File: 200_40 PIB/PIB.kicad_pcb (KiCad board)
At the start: 4 copper layers, 80 x 49 mm, 234 parts, among them J1 M80-5100442, J10 53398-0671, J11 53398-0271, J12 M80-5100842, J13 53398-0271, J15 53398-0571, J2 53398-0471, J3 G125-MS12605M2P, J4 53398-0671, J5 53398-1371, J6 MMCX, J7 MMCX, J8 SWD/DEBUG, J9 53398-0671, Q1 Si7489DP, Q10 IRF7832, Q11 IRF7832, Q2 Si7489DP, Q9 IRF7832, SW1 B3F-1000, U1 LT3065EDDPBF, U10 LT8580EDD, U11 OP37, U12 MAX823TEUK_T, U13 74LVC1G18DBV, U14 74HC08PW, U15 74HC08PW, U16 74LVC2G157DCU, U17 74LVC1G18DBV, U2 MIC4424YM, U3 MIC4424YM, U4 STM32G431RBTx, U5 ADM1270ACPZ, U6 LM1117MP-3.3, U7 ADM1270ACPZ, U8 74LVC1GU04DRL, U9 74LVC2G126DCU, Y1 ABM3B-8.000MHZ-10-D1G-T

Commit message: LADS WE ARE FUCKED
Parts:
- removed R10, R11, R12, R43, R5, R60: 1K, Resistor_SMD:R_0402_1005Metric
- removed R44: 100K, Resistor_SMD:R_0402_1005Metric
- removed R59: 33K, Resistor_SMD:R_0402_1005Metric
- removed R61: 2K, Resistor_SMD:R_0402_1005Metric
- added C69: 4.7uF, Capacitor_SMD:C_0603_1608Metric, F.Cu at (204.8, 47.1)
- added C70: 1uF, Capacitor_SMD:C_0603_1608Metric, F.Cu at (204.8, 49.6)
- added C71: 470pF, Capacitor_SMD:C_0402_1005Metric, F.Cu at (208.2, 46.9)
- added C72: 470pF, Capacitor_SMD:C_0402_1005Metric, F.Cu at (208.2, 48.8)
- added C73: 1uF, Capacitor_SMD:C_0402_1005Metric, F.Cu at (223.3, 64.9)
- added C74: 1uF, Capacitor_SMD:C_0402_1005Metric, F.Cu at (223.3, 66.8)
- added C75: 100nF, Capacitor_SMD:C_0402_1005Metric, F.Cu at (223.3, 68.8)
- added C76: 100nF, Capacitor_SMD:C_0402_1005Metric, F.Cu at (207.7, 64.9)
- added C77: 100nF, Capacitor_SMD:C_0402_1005Metric, F.Cu at (207.7, 66.8)
- added C78: 1uF, Capacitor_SMD:C_0603_1608Metric, F.Cu at (204.3, 65.1)
- added C79: 1uF, Capacitor_SMD:C_0603_1608Metric, F.Cu at (204.3, 67.6)
- added C80: 100nF, Capacitor_SMD:C_0402_1005Metric, F.Cu at (207.7, 68.8)
- added C81: 22nF, Capacitor_SMD:C_0402_1005Metric, F.Cu at (207.7, 70.8)
- added C82: 1uF, Capacitor_SMD:C_0603_1608Metric, F.Cu at (204.3, 70.2)
- added D11: NSVR1020MW2T1G, Diode_SMD:D_SOD-323, F.Cu at (214.8, 65.3)
- added D36: NSVR1020MW2T1G, Diode_SMD:D_SOD-323, F.Cu at (214.8, 68.3)
- added D37: NSVR1020MW2T1G, Diode_SMD:D_SOD-323, F.Cu at (214.8, 71.2)
- added D38: SD12C-01F, Diode_SMD:D_SOD-323, F.Cu at (195.7, 47.3)
- added D39: BAT54J, Diode_SMD:D_SOD-323F, F.Cu at (195.7, 50.3)
- added D40: BAT54J, Diode_SMD:D_SOD-323F, F.Cu at (195.7, 53.2)
- added D41: BAT54J, Diode_SMD:D_SOD-323F, F.Cu at (214.8, 74.2)
- added D42: BAT54J, Diode_SMD:D_SOD-323F, F.Cu at (214.8, 77.2)
- added D43: BAT54J, Diode_SMD:D_SOD-323F, F.Cu at (195.7, 56.2)
- added D44: BAT54J, Diode_SMD:D_SOD-323F, F.Cu at (195.7, 59.1)
- added D45: PESD3V3U1UL, Diode_SMD:D_SOD-882, F.Cu at (203.7, 75.1)
- added D46: PESD3V3U1UL, Diode_SMD:D_SOD-882, F.Cu at (203.7, 77.4)
- added D47: BAT54C, Package_TO_SOT_SMD:SOT-23, F.Cu at (219.4, 66.1)
- added D48: BAT54C, Package_TO_SOT_SMD:SOT-23, F.Cu at (219.4, 70.5)
- added D49: PESD3V3U1UL, Diode_SMD:D_SOD-882, F.Cu at (203.7, 79.8)
- added D50: BAT54C, Package_TO_SOT_SMD:SOT-23, F.Cu at (219.4, 75.0)
- added JP1: WD_ENABLE, Jumper:SolderJumper-2_P1.3mm_Open_Pad1.0x1.5mm, F.Cu at (207.2, 81.0)
- added Q3: BSS138, Package_TO_SOT_SMD:SOT-23, F.Cu at (200.3, 48.1)
- added Q4: BSS138, Package_TO_SOT_SMD:SOT-23, F.Cu at (200.3, 52.5)
- added Q5: BSS138, Package_TO_SOT_SMD:SOT-23, F.Cu at (200.3, 57.0)
- added Q6: Si7489DP, Package_SO:PowerPAK_SO-8_Single, F.Cu at (198.0, 79.1)
- added R100: 100R, Resistor_SMD:R_0402_1005Metric, F.Cu at (207.1, 56.9)
- added R101: 10K, Resistor_SMD:R_0402_1005Metric, F.Cu at (207.1, 58.9)
- added R102: 100R, Resistor_SMD:R_0402_1005Metric, F.Cu at (207.1, 60.9)
- added R103: 1K, Resistor_SMD:R_0402_1005Metric, F.Cu at (195.0, 66.9)
- added R104: 1K, Resistor_SMD:R_0402_1005Metric, F.Cu at (210.0, 56.9)
- added R105: 1K, Resistor_SMD:R_0402_1005Metric, F.Cu at (210.0, 58.9)
- added R106: 100R, Resistor_SMD:R_0402_1005Metric, F.Cu at (210.0, 60.9)
- added R107: 100K, Resistor_SMD:R_0402_1005Metric, F.Cu at (223.3, 75.4)
- added R108: 1K, Resistor_SMD:R_0402_1005Metric, F.Cu at (195.0, 68.8)
- added R109: 10K, Resistor_SMD:R_0402_1005Metric, F.Cu at (195.0, 70.8)
- added R110: 100R, Resistor_SMD:R_0402_1005Metric, F.Cu at (223.3, 77.4)
- added R111: 33K, Resistor_SMD:R_0402_1005Metric, F.Cu at (195.0, 72.8)
- added R112: 1K, Resistor_SMD:R_0402_1005Metric, F.Cu at (195.0, 74.8)
- added R113: 2K, Resistor_SMD:R_0402_1005Metric, F.Cu at (197.9, 64.9)
- added R114: 10K, Resistor_SMD:R_0402_1005Metric, F.Cu at (197.9, 66.9)
- added R115: 100K, Resistor_SMD:R_0402_1005Metric, F.Cu at (197.9, 68.8)
- added R116: 0R, Resistor_SMD:R_0402_1005Metric, F.Cu at (197.9, 70.8)
- added R117: 100K, Resistor_SMD:R_0402_1005Metric, F.Cu at (197.9, 72.8)
- added R118: 10K, Resistor_SMD:R_0402_1005Metric, F.Cu at (197.9, 74.8)
- added R119: 10K, Resistor_SMD:R_0402_1005Metric, F.Cu at (200.8, 64.9)
- added R120: 1K, Resistor_SMD:R_0402_1005Metric, F.Cu at (200.8, 66.9)
- added R121: 10K, Resistor_SMD:R_0402_1005Metric, F.Cu at (200.8, 68.8)
- added R122: 59K, Resistor_SMD:R_0402_1005Metric, F.Cu at (214.9, 54.8)
- added R123: 107K, Resistor_SMD:R_0402_1005Metric, F.Cu at (214.9, 56.8)
- added R124: 100K, Resistor_SMD:R_0402_1005Metric, F.Cu at (200.8, 70.8)
- added R125: 150K, Resistor_SMD:R_0402_1005Metric, F.Cu at (200.8, 72.8)
- added R126: 158K, Resistor_SMD:R_0402_1005Metric, F.Cu at (214.9, 46.9)
- added R127: 3.92K, Resistor_SMD:R_0402_1005Metric, F.Cu at (214.9, 48.9)
- added R128: 9.53K, Resistor_SMD:R_0402_1005Metric, F.Cu at (214.9, 50.8)
- added R88: 10K, Resistor_SMD:R_0402_1005Metric, F.Cu at (195.0, 64.9)
- added R89: 10K, Resistor_SMD:R_0402_1005Metric, F.Cu at (219.8, 46.9)
- added R90: 10K, Resistor_SMD:R_0402_1005Metric, F.Cu at (219.8, 48.9)
- added R91: 10K, Resistor_SMD:R_0402_1005Metric, F.Cu at (219.8, 50.8)
- added R92: 10K, Resistor_SMD:R_0402_1005Metric, F.Cu at (219.8, 52.8)
- added R93: 10K, Resistor_SMD:R_0402_1005Metric, F.Cu at (219.8, 54.8)
- added R94: 10K, Resistor_SMD:R_0402_1005Metric, F.Cu at (219.8, 56.8)
- added R95: 100K, Resistor_SMD:R_0603_1608Metric, F.Cu at (204.8, 52.1)
- added R96: 10K, Resistor_SMD:R_0402_1005Metric, F.Cu at (204.2, 56.9)
- added R97: 10K, Resistor_SMD:R_0402_1005Metric, F.Cu at (204.2, 58.9)
- added R98: 1M, Resistor_SMD:R_0603_1608Metric, F.Cu at (204.8, 54.6)
- added R99: 10K, Resistor_SMD:R_0402_1005Metric, F.Cu at (204.2, 60.9)
- added TH1: 3435K 10K, Resistor_SMD:R_0603_1608Metric, F.Cu at (204.3, 72.7)
- added U18: 74LVC2G14, Package_TO_SOT_SMD:SOT-23-6, F.Cu at (224.4, 72.2)
- added U19: ADM1270ACPZ, Package_CSP:LFCSP-16-1EP_3x3mm_P0.5mm_EP1.5x1.5mm, F.Cu at (208.0, 76.6)
- C26, C27: value 27pF -> 12pF
- C29, C34: value 10nF -> 100nF
- C45: value TBD -> 10nF C0G
- D18: value PESD5V0S1UL -> LED; footprint Diode_SMD:D_SOD-882 -> LED_SMD:LED_0603_1608Metric
- R17: value 1.13K -> 1K
- R18: value 21.5K -> 20K
- R35: value 15m -> 10m
- R38: value 1K -> 10m; footprint Resistor_SMD:R_0402_1005Metric -> Resistor_SMD:R_0805_2012Metric
- R45: value 10K -> 100K; footprint Resistor_SMD:R_0603_1608Metric -> Resistor_SMD:R_0402_1005Metric
- R46: value 43K -> 1K; footprint Resistor_SMD:R_0603_1608Metric -> Resistor_SMD:R_0402_1005Metric
- R47: value 1K -> 100K
- R48: value 2K -> 9.53K
- R49: value 1K -> 3.92K
- R50: value 33K -> 158K
- R57: value 33K -> 100K
- R79: value TBD -> 2K
- SW1: value B3F-1000 -> SKRKAHE020; footprint Button_Switch_THT:SW_PUSH_6mm -> Button_Switch_SMD:SW_Push_SPST_NO_Alps_SKRK
- U11: value OP37 -> OP27
- U8: value 74LVC1GU04DRL -> 74AHC1G125; footprint Package_TO_SOT_SMD:SOT-553 -> Package_TO_SOT_SMD:SOT-23-5
- U9: value 74LVC2G126DCU -> 74LVC2G17; footprint Package_SO:VSSOP-8_2.3x2mm_P0.5mm -> Package_TO_SOT_SMD:SOT-23-6
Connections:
- net /IGNITER_RST renamed /~{PD_RST}
- C1 pad 1: BAT_HOT -> VBAT_PROT
- C21 pad 1: Net-(U5-ISET) -> Net-(U5-VCAP)
- C22 pad 1: +12V -> Net-(D11-A)
- C28 pad 1: BAT_HOT -> VBAT_PROT
- C33 pad 1: BAT_HOT -> VBAT_PROT
- C45 pad 2: /ADC_I_DCHG -> Net-(Q3-S)
- C6 pad 1: +12V -> Net-(D11-A)
- C62 pad 1: BAT_HOT -> VBAT_PROT
- D18 pad 1: /ADC_V_DCHG -> GND
- D18 pad 2: GND -> Net-(D18-A)
- D3 pad 1: BAT_HOT -> VBAT_HOT
- J2 pad 2: BAT_HOT -> VBAT_PROT
- J2 pad 3: BAT_HOT -> VBAT_PROT
- J3 pad 1: BAT_HOT -> VBAT_HOT
- J3 pad 2: BAT_HOT -> VBAT_HOT
- J3 pad 3: BAT_HOT -> VBAT_HOT
- J6 pad 1: /ADC_V_DCHG -> /Rogowski Integrator/V_DCHG_IN
- J7 pad 1: Net-(J7-In) -> Net-(D38-A2)
- J8 pad 5: /nRST -> Net-(J8-Pin_5)
- R1 pad 1: BAT_HOT -> +3.3V
- R1 pad 2: Net-(U1-PWRGD) -> /12V_PG
- R18 pad 1: +12V -> Net-(D11-A)
- R29 pad 1: /IGNITER_PULSE_GATED -> /IGNITER_EXT
- R35 pad 2: BAT_HOT -> VBAT_PROT
- R38 pad 1: /VALVE1_H_GATED -> Net-(U19-SENSE-)
- R38 pad 2: Net-(U2-INB) -> VBAT_HOT
- R39 pad 1: Net-(U2-INB) -> /VALVE1_H_GATED
- R40 pad 1: Net-(U2-INA) -> /VALVE1_L_GATED
- R45 pad 1: GND -> /Valve Driver/EGSE_OPEN_F
- R45 pad 2: Net-(R45-Pad2) -> GND
- R46 pad 1: Net-(R45-Pad2) -> /Valve Driver/EGSE_OPEN_F
- R46 pad 2: 12V_GSE -> /OPEN/~{CLOSE}
- R47 pad 1: /OPEN/~{CLOSE} -> Net-(D41-K)
- R47 pad 2: Net-(Q10-G) -> GND
- R50 pad 2: BAT_HOT -> VBAT_PROT
- R65 pad 2: BAT_HOT -> VBAT_PROT
- R79 pad 1: Net-(J7-In) -> Net-(C69-Pad2)
- R82 pad 1: /RCC_LSCO -> /DPT_MCLK
- R86 pad 1: /RCC_LSCO -> /DPT_MCLK
- SW1 pad 1: GND -> Net-(U12-~{MR})
- SW1 pad 2: Net-(U12-~{MR}) -> GND
- U1 pad 1: BAT_HOT -> VBAT_PROT
- U1 pad 10: +12V -> Net-(D11-A)
- U1 pad 2: BAT_HOT -> VBAT_PROT
- U1 pad 3: BAT_HOT -> VBAT_PROT
- U1 pad 4: Net-(U1-PWRGD) -> /12V_PG
- U1 pad 9: +12V -> Net-(D11-A)
- U11 pad 3: GND -> Net-(U11A-+)
- U11 pad 6: /ADC_I_DCHG -> Net-(Q3-S)
- U12 pad 4: /WDG_IN -> Net-(JP1-B)
- U2 pad 2: Net-(U2-INA) -> /VALVE1_L_GATED
- U2 pad 4: Net-(U2-INB) -> /VALVE1_H_GATED
- U4 pad 14: /RCC_LSCO -> /12V_PG
- U4 pad 39: unconnected-(U4-PC7-Pad39) -> /DPT_MCLK
- U4 pad 44: unconnected-(U4-PA10-Pad44) -> /BAT_EN
- U4 pad 45: unconnected-(U4-PA11-Pad45) -> /BAT_PGOOD
- U4 pad 55: unconnected-(U4-PD2-Pad55) -> /DEBUG_LED
- U5 pad 1: Net-(U5-ISET) -> Net-(U5-VCAP)
- U5 pad 15: BAT_HOT -> VBAT_PROT
- U7 pad 15: BAT_HOT -> VBAT_PROT
- U8 pad 1: unconnected-(U8-NC-Pad1) -> GND
- U8 pad 2: Net-(R43-Pad2) -> /IGNITER_PULSE_GATED
- U8 pad 4: Net-(U8-Pad4) -> /IGNITER_EXT
- U8 pad 5: 3.3V_EGSE -> +3.3V
- U9 pad 1: Net-(R45-Pad2) -> Net-(D42-K)
- U9 pad 2: Net-(R43-Pad2) -> GND
- U9 pad 3: Net-(U3-INA) -> Net-(D41-K)
- U9 pad 4: GND -> Net-(D47-Pad1)
- U9 pad 5: Net-(U8-Pad4) -> 3.3V_EGSE
- U9 pad 6: Net-(U3-INB) -> Net-(D48-Pad1)
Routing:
- net (no net): track 0.00 -> 63.3 mm, vias 0 -> 3
- net /RCC_LSCO: track 34.3 -> 0.00 mm, vias 2 -> 0
- net VBAT_PROT: track 0.00 -> 16.5 mm, vias 0 -> 10
- net BAT_HOT: track 16.5 -> 0.00 mm, vias 10 -> 0
- net Net-(R43-Pad2): track 14.9 -> 0.00 mm
- net Net-(R45-Pad2): track 5.08 -> 0.00 mm, vias 1 -> 0
- net Net-(J7-In): track 3.21 -> 0.00 mm
- net Net-(U8-Pad4): track 3.11 -> 0.00 mm
- net Net-(U2-INA): track 2.94 -> 0.00 mm
- net /VALVE1_L_GATED: track 28.3 -> 31.3 mm
- net Net-(U2-INB): track 2.67 -> 0.00 mm
- net Net-(U1-PWRGD): track 2.14 -> 0.00 mm
- net /12V_PG: track 0.00 -> 2.14 mm
- net Net-(U11A-+): vias 0 -> 1
- net Net-(D18-A): vias 0 -> 1
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- added copper zone on F.Cu, net VBAT_HOT
- added copper zone on B.Cu, net VBAT_PROT
- removed copper zone on B.Cu, net BAT_HOT
- removed copper zone on F.Cu, net BAT_HOT

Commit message: sync board
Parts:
- D41: moved to B.Cu
- moved D42 79.6 mm to (247.0, 150.0)
- moved D41 63.2 mm to (241.5, 131.5)
- moved SW1 4.62 mm to (210.5, 118.5)
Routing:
- net (no net): track 63.3 -> 41.5 mm
- net Net-(U12-~{MR}): track 48.3 -> 39.8 mm
- net Net-(U3-INB): track 18.1 -> 9.98 mm
- net Net-(U3-INA): track 14.6 -> 7.01 mm
- net 3.3V_EGSE: track 13.0 -> 8.91 mm

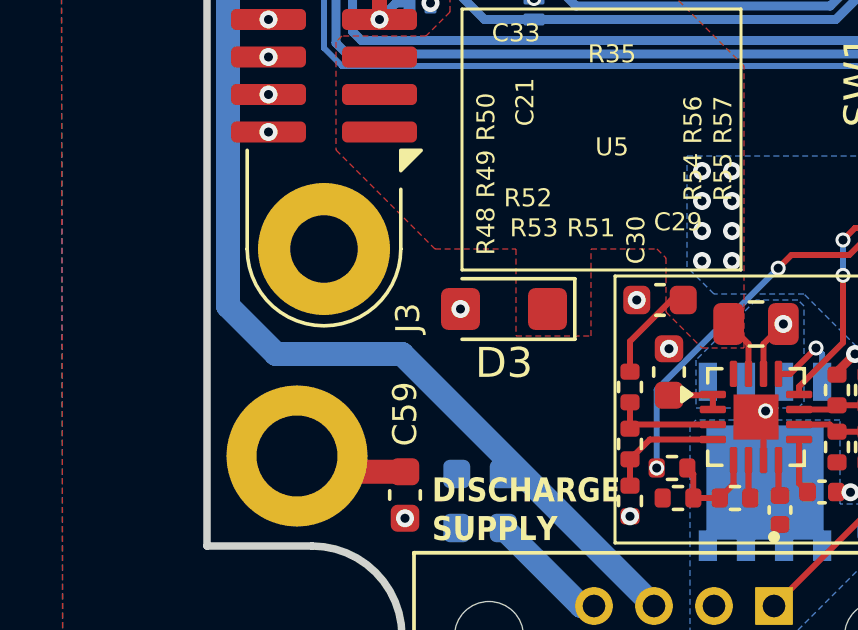
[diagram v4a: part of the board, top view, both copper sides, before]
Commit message: correct 3d model paths
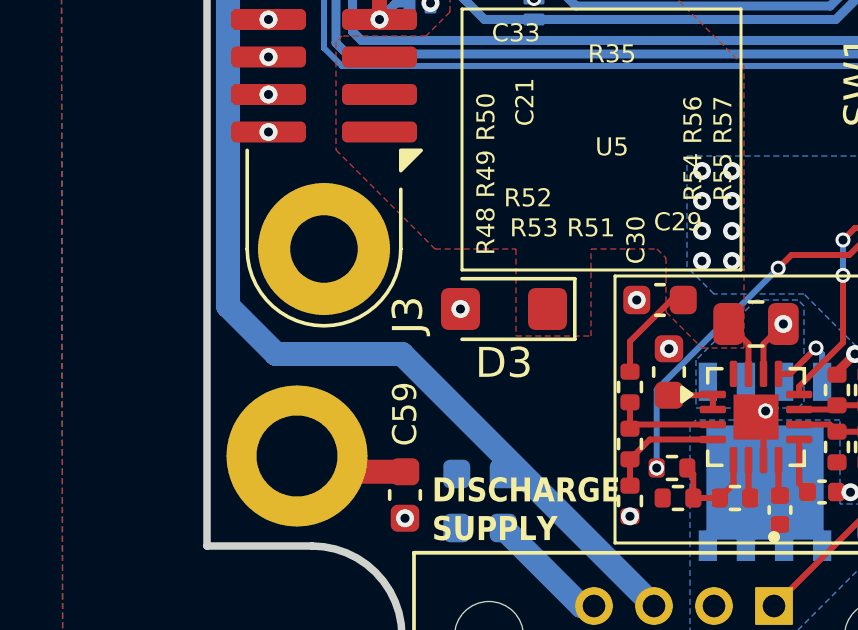
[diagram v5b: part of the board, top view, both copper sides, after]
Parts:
- J3: footprint Connector_Harwin:Harwin_Gecko_G125-MS12605M2P_2x13_P1.25mm_Vertical -> 0_PAY_Footprint_Library:Harwin_Gecko_G125-MS12605M2P_2x13_P1.25mm_Vertical
- Q1, Q2, Q6: footprint Package_SO:PowerPAK_SO-8_Single -> 0_PAY_Footprint_Library:PowerPAK_SO-8_Single
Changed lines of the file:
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@@
 				(name "A")
 				(pins "28" "7" "5" "6" "55" "8" "9" "10" "11" "22" "23" "38" "39" "40"
-					"41" "52" "53" "54" "2" "3" "4" "1" "16" "32" "47" "15" "63" "31" "48"
+					"41" "52" "53" "54" "2" "3" "4" "1" "16" "32" "31" "63" "15" "47" "48"
 					"27" "64" "29" "12" "13" "14" "17" "18" "19" "20" "21" "42" "43" "44"
 					"45" "46" "49" "50" "51" "24" "25" "26" "56" "57" "58" "59" "60" "61"
@@
 		)
 	)
-	(footprint "Connector_Harwin:Harwin_Gecko_G125-MS12605M2P_2x13_P1.25mm_Vertical"
+	(footprint "0_PAY_Footprint_Library:Harwin_Gecko_G125-MS12605M2P_2x13_P1.25mm_Vertical"
 		(layer "F.Cu")
 		(at 190.4 112.7 90)
@@
 		(tags "connector Harwin Gecko vertical")
 		(property "Reference" "J3"
-			(at -13.7 2.8 90)
+			(at -13.6 2.8 90)
 			(layer "F.SilkS")
 			(effects
 				(font
-					(size 0.8 0.8)
+					(size 1 1)
 					(thickness 0.15)
 				)
@@
 			(effects
 				(font
-					(size 0.8 0.8)
+					(size 1 1)
 					(thickness 0.15)
 				)
@@
 		)
 	)
-	(footprint "Package_SO:PowerPAK_SO-8_Single"
+	(footprint "0_PAY_Footprint_Library:PowerPAK_SO-8_Single"
 		(layer "F.Cu")
 		(at 198.02 79.09)
@@
 			)
 		)
-		(property "Datasheet" "https://www.vishay.com/docs/65596/si7141dp.pdf"
+		(property "Datasheet" "https://www.vishay.com/docs/73436/si7489dp.pdf"
 			(at 0 0 0)
 			(unlocked yes)
@@
 			)
 		)
-		(property "Description" "-60A Id, -20V Vds, 1.9 mOhm Ron, PowerPAK-8"
+		(property "Description" "-28A Id, -100V Vds, 33mOhm Rdson"
 			(at 0 0 0)
 			(unlocked yes)
@@
 		)
 		(embedded_fonts no)
-		(model "${KICAD10_3DMODEL_DIR}/Package_SO.3dshapes/PowerPAK_SO-8_Single.step"
+		(model "${KIPRJMOD}/../0_PAY_3D_Model_Library/PowerPakSO-8.STEP"
 			(offset
 				(xyz 0 0 0)
@@
 			)
 			(rotate
-				(xyz 0 0 0)
+				(xyz -90 -0 -0)
 			)
 		)
@@
 		)
 	)
-	(footprint "Package_SO:PowerPAK_SO-8_Single"
+	(footprint "0_PAY_Footprint_Library:PowerPAK_SO-8_Single"
 		(layer "B.Cu")
 		(at 205.1 131.195 -90)
@@
 			(effects
 				(font
-					(size 0.8 0.8)
+					(size 1 1)
 					(thickness 0.15)
 				)
@@
 			)
 		)
-		(property "Datasheet" "https://www.vishay.com/docs/65596/si7141dp.pdf"
+		(property "Datasheet" "https://www.vishay.com/docs/73436/si7489dp.pdf"
 			(at 0 0 90)
 			(unlocked yes)
@@
 			)
 		)
-		(property "Description" "-60A Id, -20V Vds, 1.9 mOhm Ron, PowerPAK-8"
+		(property "Description" "-28A Id, -100V Vds, 33mOhm Rdson"
 			(at 0 0 90)
 			(unlocked yes)
@@
 			(effects
 				(font
-					(size 0.8 0.8)
+					(size 1 1)
 					(thickness 0.15)
 				)
@@
 		)
 		(embedded_fonts no)
-		(model "${KICAD10_3DMODEL_DIR}/Package_SO.3dshapes/PowerPAK_SO-8_Single.step"
+		(model "${KIPRJMOD}/../0_PAY_3D_Model_Library/PowerPakSO-8.STEP"
 			(offset
 				(xyz 0 0 0)
@@
 			)
 			(rotate
-				(xyz 0 0 0)
+				(xyz -90 -0 -0)
 			)
 		)
@@
 		)
 	)
-	(footprint "Package_SO:PowerPAK_SO-8_Single"
+	(footprint "0_PAY_Footprint_Library:PowerPAK_SO-8_Single"
 		(layer "B.Cu")
 		(at 204.6 99.95)
@@
 		(tags "PowerPAK SO-8 Single")
 		(property "Reference" "Q2"
-			(at 4.1 1.55 90)
+			(at 0 3.5 180)
 			(layer "B.SilkS")
 			(effects
 				(font
-					(size 0.8 0.8)
+					(size 1 1)
 					(thickness 0.15)
 				)
@@
 		)
 		(property "Value" "Si7489DP"
-			(at 0 -3.5 0)
+			(at 0 -3.5 180)
 			(layer "B.Fab")
 			(effects
@@
 			)
 		)
-		(property "Datasheet" "https://www.vishay.com/docs/65596/si7141dp.pdf"
+		(property "Datasheet" "https://www.vishay.com/docs/73436/si7489dp.pdf"
 			(at 0 0 180)
 			(unlocked yes)
@@
 			)
 		)
-		(property "Description" "-60A Id, -20V Vds, 1.9 mOhm Ron, PowerPAK-8"
+		(property "Description" "-28A Id, -100V Vds, 33mOhm Rdson"
 			(at 0 0 180)
 			(unlocked yes)
@@
 		)
 		(fp_text user "${REFERENCE}"
-			(at 0 0 0)
+			(at 0 0 180)
 			(layer "B.Fab")
 			(effects
 				(font
-					(size 0.8 0.8)
+					(size 1 1)
 					(thickness 0.15)
 				)
@@
 		)
 		(embedded_fonts no)
-		(model "${KICAD10_3DMODEL_DIR}/Package_SO.3dshapes/PowerPAK_SO-8_Single.step"
+		(model "${KIPRJMOD}/../0_PAY_3D_Model_Library/PowerPakSO-8.STEP"
 			(offset
 				(xyz 0 0 0)
@@
 			)
 			(rotate
-				(xyz 0 0 0)
+				(xyz -90 -0 -0)
 			)
 		)
@@
 		)
 		(embedded_fonts no)
-		(model "C:/Users/alanj/Documents/GitHub/payload-electrical/0_PAY_3D_Model_Library/LT8580EDD_PBF.step"
+		(model "${KIPRJMOD}/../0_PAY_3D_Model_Library/LT8580EDD_PBF.step"
 			(offset
 				(xyz 0 0 0)
@@
 		)
 		(embedded_fonts no)
-		(model "C:/Users/alanj/Documents/GitHub/payload-electrical/0_PAY_3D_Model_Library/LT3065EDDPBF.step"
+		(model "${KIPRJMOD}/../0_PAY_3D_Model_Library/LT3065EDDPBF.step"
 			(offset
 				(xyz 0 0 0)

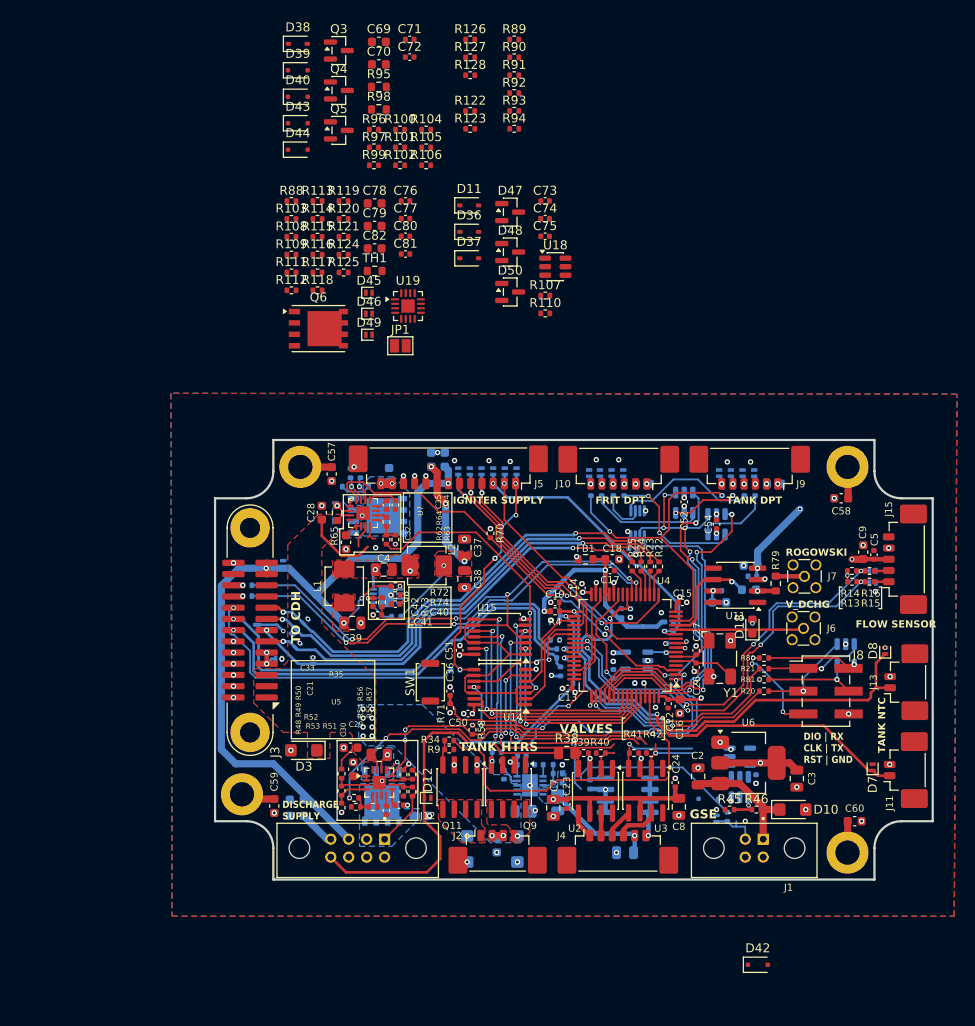
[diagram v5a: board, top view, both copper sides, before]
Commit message: select lower leakage part for integrator reset
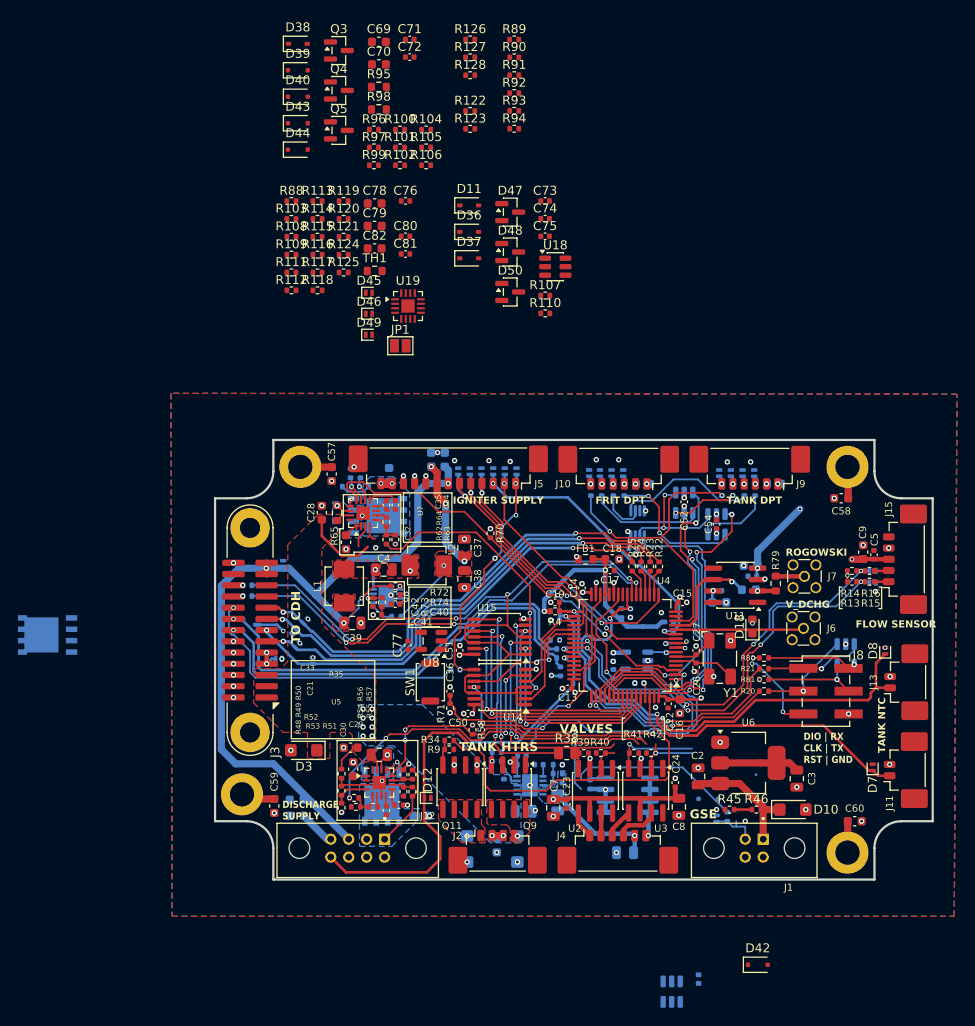
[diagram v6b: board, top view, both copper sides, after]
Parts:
- Q6: moved to B.Cu
- U8: moved to F.Cu
- moved C77 47.6 mm to (208.0, 114.4), turned to 90 degrees
- moved Q6 45.6 mm to (167.8, 113.2), turned to 180 degrees
- moved U8 36.7 mm to (210.6, 113.9), turned to 180 degrees
- moved U9 24.0 mm to (237.4, 153.0)
- moved C31 23.2 mm to (240.4, 151.6)
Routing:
- net GND: vias 111 -> 108
- net 3.3V_EGSE: vias 1 -> 0
- net (no net): vias 3 -> 2
